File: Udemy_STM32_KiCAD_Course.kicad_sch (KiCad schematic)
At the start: 19 parts, among them J1 USB_B_Micro, J2 Conn_01x04_Pin, SW1 SW_SPDT, U1 STM32F103C8T6, Y1 16MHz

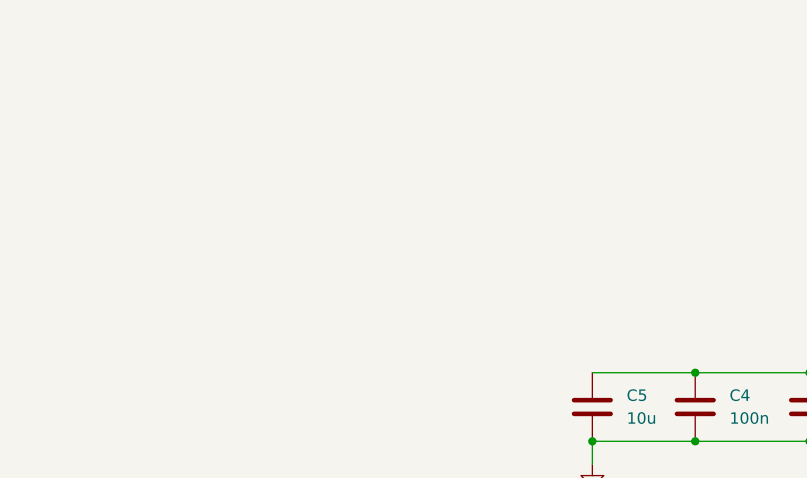
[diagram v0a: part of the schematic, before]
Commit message: added voltage regulator
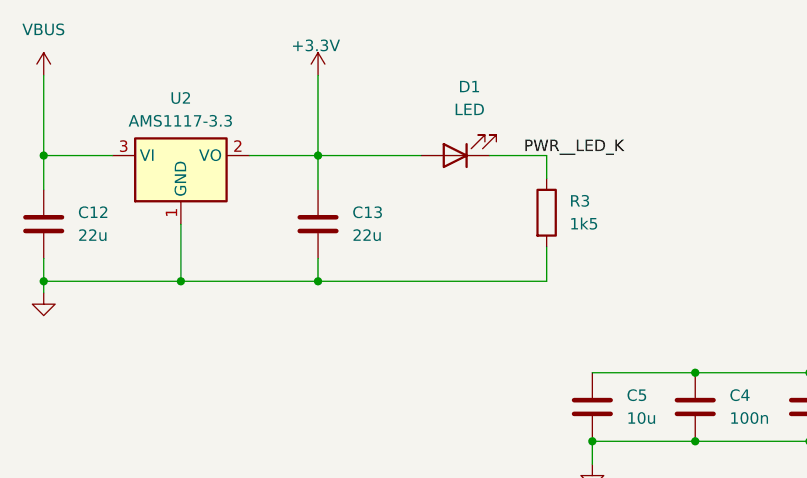
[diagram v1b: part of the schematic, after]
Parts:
- added C12, C13: 22u, symbol Device:C
- added D1: LED, symbol Device:LED
- added R3: 1k5, symbol Device:R
- added U2: AMS1117-3.3, Package_TO_SOT_SMD:SOT-223-3_TabPin2, symbol Regulator_Linear:AMS1117-3.3
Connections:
- net +3.3V: now also C13.1, D1.2 (A), U2.2 (VO)
- net GND: now also C12.2, C13.2, R3.2, U2.1 (GND)
- net VBUS: now also C12.1, U2.3 (VI)
- new net PWR__LED_K: D1.1 (K), R3.1

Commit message: complete schematic and annotations
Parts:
- added J2, J4: Conn_01x04_Pin, Connector_PinHeader_2.54mm:PinHeader_1x04_P2.54mm_Vertical, symbol Connector:Conn_01x04_Pin
- added R4, R5: 1k5, Resistor_SMD:R_0402_1005Metric, symbol Device:R
- C1: renamed from C12; footprint (none) -> Capacitor_SMD:C_0805_2012Metric
- C10: renamed from C8; footprint (none) -> Capacitor_SMD:C_0402_1005Metric
- C11: renamed from C9; footprint (none) -> Capacitor_SMD:C_0402_1005Metric
- C12: renamed from C10; footprint (none) -> Capacitor_SMD:C_0402_1005Metric
- C13: renamed from C11; footprint (none) -> Capacitor_SMD:C_0402_1005Metric
- C2: renamed from C13; footprint (none) -> Capacitor_SMD:C_0805_2012Metric
- C3: renamed from C5; footprint (none) -> Capacitor_SMD:C_0603_1608Metric
- C4: footprint (none) -> Capacitor_SMD:C_0402_1005Metric
- C5: renamed from C3; footprint (none) -> Capacitor_SMD:C_0402_1005Metric
- C6: renamed from C2; footprint (none) -> Capacitor_SMD:C_0402_1005Metric
- C7: renamed from C1; footprint (none) -> Capacitor_SMD:C_0402_1005Metric
- C8: renamed from C6; footprint (none) -> Capacitor_SMD:C_0402_1005Metric
- C9: renamed from C7; footprint (none) -> Capacitor_SMD:C_0402_1005Metric
- D1: footprint (none) -> LED_SMD:LED_0603_1608Metric
- FB1: footprint (none) -> Inductor_SMD:L_0603_1608Metric
- J1: footprint (none) -> Connector_USB:USB_Micro-B_Wuerth_629105150521
- J3: renamed from J2; footprint (none) -> Connector_PinHeader_2.54mm:PinHeader_1x04_P2.54mm_Vertical
- R1: renamed from R3; footprint (none) -> Resistor_SMD:R_0402_1005Metric
- R2: renamed from R1; footprint (none) -> Resistor_SMD:R_0402_1005Metric
- R3: renamed from R2; footprint (none) -> Resistor_SMD:R_0402_1005Metric
- SW1: footprint (none) -> Button_Switch_THT:SW_E-Switch_EG1224_SPDT_Angled
- Y1: footprint (none) -> Crystal:Crystal_SMD_3225-4Pin_3.2x2.5mm
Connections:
- net +3.3V: now also J3.1 (Pin_1), R3.2, J2.1 (Pin_1), J4.1 (Pin_1), R4.1, R5.1
- net +3.3VA: no longer J3.1 (Pin_1), R3.2
- net GND: now also J2.4 (Pin_4), J4.4 (Pin_4)
- net I2C2_SCL: now reaches U1.21 (PB10)
- net I2C2_SCL: now also J4.2 (Pin_2), R4.2
- net I2C2_SDA: now reaches U1.22 (PB11)
- net I2C2_SDA: now also J4.3 (Pin_3), R5.2
- net USART1_TX: now reaches U1.42 (PB6)
- net USART1_TX: now also J2.2 (Pin_2)
- net USART1_RX: now reaches U1.43 (PB7)
- net USART1_RX: now also J2.3 (Pin_3)
- no-connect marks 2 -> 29
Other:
- note added: "1 100nF capacitor per VDD pin"
- note added: "CL = 2* (CL0 - CS) = 2 * (10 - 5) pF"
- note added: "Microcontroller and USB"
- note added: "Pin out using STM32 Cube IDE"
- note added: "Power Supply"
- note added: "UDEMY STM32 DEMO PCB"
- note added: "USB App note AN4879"
- note added: "VBUS from USB connector (nom. 5V). Min 22uF input/output capacitor"
- note added: "VDDA filtering"
- title: (none) -> Udemy STM32 Demo PCB
- moved on the sheet: C1, C10, C11, C12, C13, C2, C3, C4, C5, C6, C7, C8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

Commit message: Completed layout and routing
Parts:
- added H1, H2, H3, H4: MountingHole, MountingHole:MountingHole_2.2mm_M2, symbol Mechanical:MountingHole
- SW1: footprint Button_Switch_THT:SW_E-Switch_EG1224_SPDT_Angled -> Button_Switch_SMD:SW_SPDT_PCM12
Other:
- note added: "M2"
- note added: "Mounting Holes"
- note added: "Refer to AN2867 - STM Oscillator Design Guide"
